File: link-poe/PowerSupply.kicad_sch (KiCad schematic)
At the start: 8 parts, among them U501 TPSM33625

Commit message: Update Library
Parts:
- C501: symbol V2_Device:C_1210_10u -> V2_Capacitor:1210_10u
- C502: symbol V2_Device:C_0603_0u1 -> V2_Capacitor:0603_0u1
- C503, C504: value 22u -> 10u; symbol V2_Device:C_1210_22u -> V2_Capacitor:1210_22u
- C505: symbol V2_Device:C_0603_1u -> V2_Capacitor:0603_1u
- R501: symbol V2_Device:R_0603_40k2 -> V2_Resistor:0603_40k2
- R502: symbol V2_Device:R_0603_10k -> V2_Resistor:0603_10k
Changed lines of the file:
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@@
 	)
 	(symbol
-		(lib_id "V2_Device:C_0603_0u1")
+		(lib_id "V2_Capacitor:0603_0u1")
 		(at 109.22 97.79 0)
 		(unit 1)
@@
 	)
 	(symbol
-		(lib_id "V2_Device:C_1210_22u")
+		(lib_id "V2_Capacitor:1210_22u")
 		(at 195.58 97.79 0)
 		(unit 1)
@@
 			)
 		)
-		(property "Value" "22u"
+		(property "Value" "10u"
 			(at 198.12 99.06 0)
 			(effects
@@
 	)
 	(symbol
-		(lib_id "V2_Device:R_0603_40k2")
+		(lib_id "V2_Resistor:0603_40k2")
 		(at 172.72 97.79 0)
 		(unit 1)
@@
 		(on_board yes)
 		(dnp no)
-		(property "Reference" "#PWR0504"
+		(property "Reference" "#PWR504"
 			(at 185.42 106.68 0)
 			(effects
@@
 			(project "power-rj45"
 				(path "/6c8448b4-b04d-47e1-934e-e40cbe27a7be/24a9dc0c-cb3c-464a-a734-f09bf949d71a"
-					(reference "#PWR0504")
+					(reference "#PWR504")
 					(unit 1)
 				)
@@
 		(on_board yes)
 		(dnp no)
-		(property "Reference" "#PWR0505"
+		(property "Reference" "#PWR505"
 			(at 195.58 106.68 0)
 			(effects
@@
 			(project "power-rj45"
 				(path "/6c8448b4-b04d-47e1-934e-e40cbe27a7be/24a9dc0c-cb3c-464a-a734-f09bf949d71a"
-					(reference "#PWR0505")
+					(reference "#PWR505")
 					(unit 1)
 				)
@@
 		(on_board yes)
 		(dnp no)
-		(property "Reference" "#PWR0501"
+		(property "Reference" "#PWR501"
 			(at 195.58 99.06 0)
 			(effects
@@
 			(project "power-rj45"
 				(path "/6c8448b4-b04d-47e1-934e-e40cbe27a7be/24a9dc0c-cb3c-464a-a734-f09bf949d71a"
-					(reference "#PWR0501")
+					(reference "#PWR501")
 					(unit 1)
 				)
@@
 		(on_board yes)
 		(dnp no)
-		(property "Reference" "#PWR0502"
+		(property "Reference" "#PWR502"
 			(at 97.79 106.68 0)
 			(effects
@@
 			(project "power-rj45"
 				(path "/6c8448b4-b04d-47e1-934e-e40cbe27a7be/24a9dc0c-cb3c-464a-a734-f09bf949d71a"
-					(reference "#PWR0502")
+					(reference "#PWR502")
 					(unit 1)
 				)
@@
 		(on_board yes)
 		(dnp no)
-		(property "Reference" "#PWR0506"
+		(property "Reference" "#PWR506"
 			(at 172.72 111.76 0)
 			(effects
@@
 			(project "power-rj45"
 				(path "/6c8448b4-b04d-47e1-934e-e40cbe27a7be/24a9dc0c-cb3c-464a-a734-f09bf949d71a"
-					(reference "#PWR0506")
+					(reference "#PWR506")
 					(unit 1)
 				)
@@
 		(on_board yes)
 		(dnp no)
-		(property "Reference" "#PWR0503"
+		(property "Reference" "#PWR503"
 			(at 109.22 106.68 0)
 			(effects
@@
 			(project "power-rj45"
 				(path "/6c8448b4-b04d-47e1-934e-e40cbe27a7be/24a9dc0c-cb3c-464a-a734-f09bf949d71a"
-					(reference "#PWR0503")
-					(unit 1)
-				)
-			)
-		)
-	)
-	(symbol
-		(lib_id "V2_Device:C_0603_1u")
+					(reference "#PWR503")
+					(unit 1)
+				)
+			)
+		)
+	)
+	(symbol
+		(lib_id "V2_Capacitor:0603_1u")
 		(at 128.27 107.95 0)
 		(unit 1)
@@
 	)
 	(symbol
-		(lib_id "V2_Device:C_1210_22u")
+		(lib_id "V2_Capacitor:1210_22u")
 		(at 185.42 97.79 0)
 		(unit 1)
@@
 			)
 		)
-		(property "Value" "22u"
+		(property "Value" "10u"
 			(at 187.96 99.06 0)
 			(effects
@@
 		(on_board yes)
 		(dnp no)
-		(property "Reference" "#PWR0507"
+		(property "Reference" "#PWR507"
 			(at 128.27 116.84 0)
 			(effects
@@
 			(project "power-rj45"
 				(path "/6c8448b4-b04d-47e1-934e-e40cbe27a7be/24a9dc0c-cb3c-464a-a734-f09bf949d71a"
-					(reference "#PWR0507")
-					(unit 1)
-				)
-			)
-		)
-	)
-	(symbol
-		(lib_id "V2_Device:R_0603_10k")
+					(reference "#PWR507")
+					(unit 1)
+				)
+			)
+		)
+	)
+	(symbol
+		(lib_id "V2_Resistor:0603_10k")
 		(at 172.72 102.87 0)
 		(unit 1)
@@
 		(on_board yes)
 		(dnp no)
-		(property "Reference" "#PWR0508"
+		(property "Reference" "#PWR508"
 			(at 148.59 121.92 0)
 			(effects
@@
 			(project "power-rj45"
 				(path "/6c8448b4-b04d-47e1-934e-e40cbe27a7be/24a9dc0c-cb3c-464a-a734-f09bf949d71a"
-					(reference "#PWR0508")
-					(unit 1)
-				)
-			)
-		)
-	)
-	(symbol
-		(lib_id "V2_Device:C_1210_10u")
+					(reference "#PWR508")
+					(unit 1)
+				)
+			)
+		)
+	)
+	(symbol
+		(lib_id "V2_Capacitor:1210_10u")
 		(at 97.79 97.79 0)
 		(unit 1)

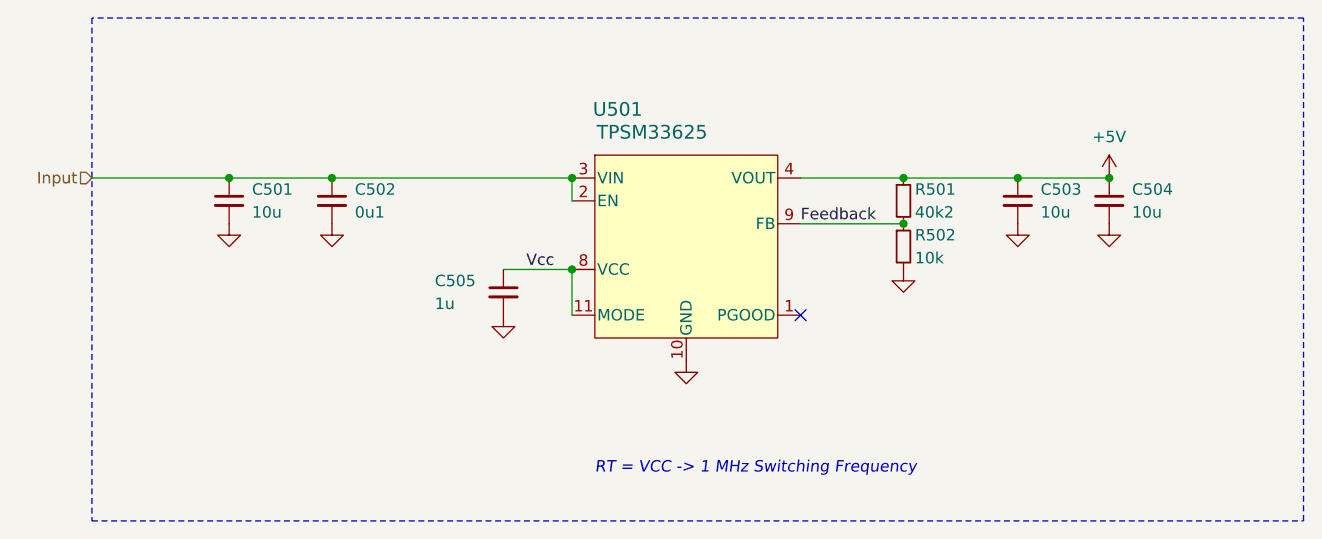
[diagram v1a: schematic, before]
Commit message: Replace step-down
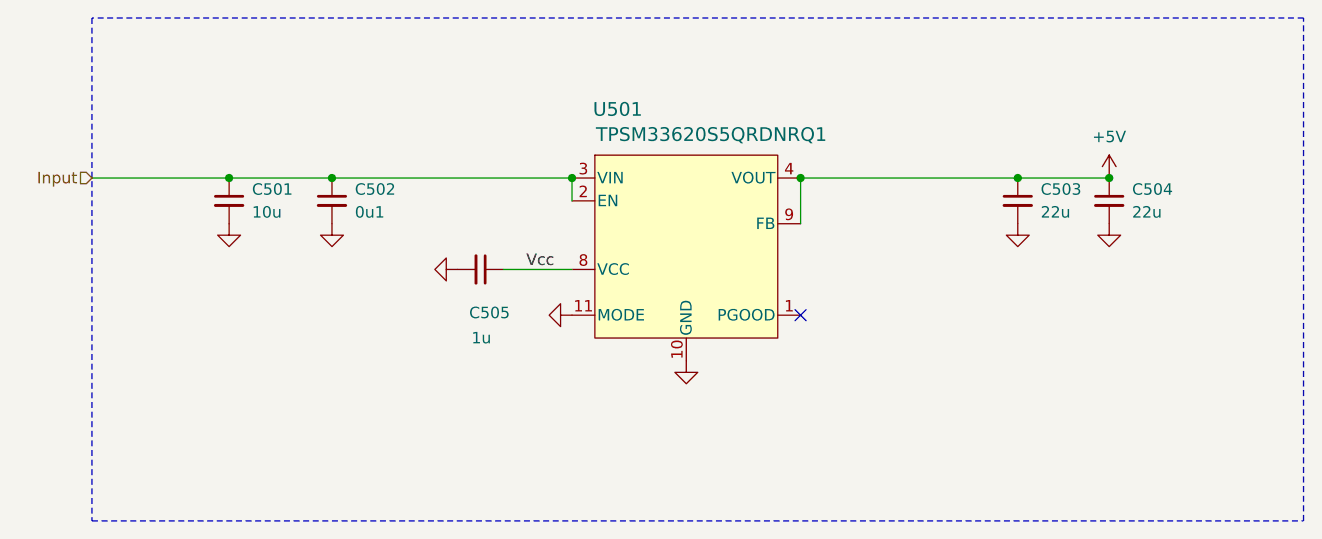
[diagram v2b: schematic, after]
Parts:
- removed R501: 40k2, V2_Resistor_SMD:R_0603, symbol V2_Resistor:0603_40k2
- removed R502: 10k, V2_Resistor_SMD:R_0603, symbol V2_Resistor:0603_10k
- C503, C504: value 10u -> 22u
- U501: value TPSM33625 -> TPSM33620S5QRDNRQ1; symbol V2_Converter_DCDC:TPSM33625RDNR -> V2_Converter_DCDC:TPSM33620S5QRDNRQ1; Mouser 595-TPSM33625RDNR -> 595-SM33620S5QRDNRQ1; Product TPSM33625RDNR -> TPSM33620S5QRDNRQ1; Rating 2.5A -> 2A
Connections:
- net Feedback is gone; now on net +5V: U501.9 (FB)
- net GND: now also U501.11 (MODE)
- net Vcc: no longer U501.11 (MODE)
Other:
- note removed: "RT = VCC -> 1 MHz Switching Frequency"
- title: Power Supply -> V2 Link PoE
- moved on the sheet: C505

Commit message: Update
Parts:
- C501: Id (none) -> Capacitor:${SYMBOL_NAME}; Mouser 810-CNA6P1X7R1H106K2 -> 810-CNC6P1X7R1H106K2; Product CNA6P1X7R1H106K250AE -> CNC6P1X7R1H106K250AE
- C502: Id (none) -> Capacitor:${SYMBOL_NAME}
- C503: renamed from C505; Id (none) -> Capacitor:${SYMBOL_NAME}
- C504: renamed from C503; Id (none) -> Capacitor:${SYMBOL_NAME}
- C505: renamed from C504; Id (none) -> Capacitor:${SYMBOL_NAME}
- U501: Id (none) -> DCDC:${SYMBOL_NAME}
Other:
- company: +5V -> Versio Duo
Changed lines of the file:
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@@
 	(title_block
 		(title "V2 Link PoE")
-		(date "2026-03-31")
+		(date "2026-04-14")
 		(rev "2026-03-31")
-		(company "+5V")
+		(company "Versio Duo")
+		(comment 1 "CAT Cable Power Supply")
 	)
 	(junction
@@
 			)
 		)
+		(property "Id" "DCDC:${SYMBOL_NAME}"
+			(at 148.59 147.32 0)
+			(hide yes)
+			(show_name no)
+			(do_not_autoplace no)
+			(effects
+				(font
+					(size 1.27 1.27)
+				)
+			)
+		)
 		(pin "1"
 		)
@@
 		(in_pos_files yes)
 		(dnp no)
-		(property "Reference" "#PWR509"
+		(property "Reference" "#PWR504"
 			(at 129.54 110.49 0)
 			(hide yes)
@@
 			(project "link-poe"
 				(path "/6c8448b4-b04d-47e1-934e-e40cbe27a7be/24a9dc0c-cb3c-464a-a734-f09bf949d71a"
-					(reference "#PWR509")
+					(reference "#PWR504")
 					(unit 1)
 				)
@@
 			)
 		)
+		(property "Id" "Capacitor:${SYMBOL_NAME}"
+			(at 109.22 113.03 0)
+			(hide yes)
+			(show_name no)
+			(do_not_autoplace no)
+			(effects
+				(font
+					(size 1.27 1.27)
+				)
+			)
+		)
 		(pin "1"
 		)
@@
 		(in_pos_files yes)
 		(dnp no)
-		(property "Reference" "C504"
+		(property "Reference" "C505"
 			(at 198.12 96.52 0)
 			(show_name no)
@@
 		(property "Rating" "25V"
 			(at 195.58 118.11 0)
+			(hide yes)
+			(show_name no)
+			(do_not_autoplace no)
+			(effects
+				(font
+					(size 1.27 1.27)
+				)
+			)
+		)
+		(property "Id" "Capacitor:${SYMBOL_NAME}"
+			(at 195.58 113.03 0)
 			(hide yes)
 			(show_name no)
@@
 			(project "link-poe"
 				(path "/6c8448b4-b04d-47e1-934e-e40cbe27a7be/24a9dc0c-cb3c-464a-a734-f09bf949d71a"
-					(reference "C504")
+					(reference "C505")
 					(unit 1)
 				)
@@
 		(in_pos_files yes)
 		(dnp no)
-		(property "Reference" "#PWR504"
+		(property "Reference" "#PWR506"
 			(at 185.42 106.68 0)
 			(hide yes)
@@
 			(project "link-poe"
 				(path "/6c8448b4-b04d-47e1-934e-e40cbe27a7be/24a9dc0c-cb3c-464a-a734-f09bf949d71a"
-					(reference "#PWR504")
+					(reference "#PWR506")
 					(unit 1)
 				)
@@
 		(in_pos_files yes)
 		(dnp no)
-		(property "Reference" "#PWR505"
+		(property "Reference" "#PWR508"
 			(at 195.58 106.68 0)
 			(hide yes)
@@
 			(project "link-poe"
 				(path "/6c8448b4-b04d-47e1-934e-e40cbe27a7be/24a9dc0c-cb3c-464a-a734-f09bf949d71a"
-					(reference "#PWR505")
+					(reference "#PWR508")
 					(unit 1)
 				)
@@
 		(in_pos_files yes)
 		(dnp no)
-		(property "Reference" "#PWR501"
+		(property "Reference" "#PWR507"
 			(at 195.58 99.06 0)
 			(hide yes)
@@
 			(project "link-poe"
 				(path "/6c8448b4-b04d-47e1-934e-e40cbe27a7be/24a9dc0c-cb3c-464a-a734-f09bf949d71a"
-					(reference "#PWR501")
+					(reference "#PWR507")
 					(unit 1)
 				)
@@
 		(in_pos_files yes)
 		(dnp no)
-		(property "Reference" "#PWR502"
+		(property "Reference" "#PWR501"
 			(at 97.79 106.68 0)
 			(hide yes)
@@
 			(project "link-poe"
 				(path "/6c8448b4-b04d-47e1-934e-e40cbe27a7be/24a9dc0c-cb3c-464a-a734-f09bf949d71a"
-					(reference "#PWR502")
+					(reference "#PWR501")
 					(unit 1)
 				)
@@
 		(in_pos_files yes)
 		(dnp no)
-		(property "Reference" "#PWR503"
+		(property "Reference" "#PWR502"
 			(at 109.22 106.68 0)
 			(hide yes)
@@
 			(project "link-poe"
 				(path "/6c8448b4-b04d-47e1-934e-e40cbe27a7be/24a9dc0c-cb3c-464a-a734-f09bf949d71a"
-					(reference "#PWR503")
+					(reference "#PWR502")
 					(unit 1)
 				)
@@
 		(in_pos_files yes)
 		(dnp no)
-		(property "Reference" "C505"
+		(property "Reference" "C503"
 			(at 124.46 110.236 90)
 			(show_name no)
@@
 		(property "Rating" "50V"
 			(at 102.87 105.41 0)
+			(hide yes)
+			(show_name no)
+			(do_not_autoplace no)
+			(effects
+				(font
+					(size 1.27 1.27)
+				)
+			)
+		)
+		(property "Id" "Capacitor:${SYMBOL_NAME}"
+			(at 110.49 105.41 0)
 			(hide yes)
 			(show_name no)
@@
 			(project "link-poe"
 				(path "/6c8448b4-b04d-47e1-934e-e40cbe27a7be/24a9dc0c-cb3c-464a-a734-f09bf949d71a"
-					(reference "C505")
+					(reference "C503")
 					(unit 1)
 				)
@@
 		(in_pos_files yes)
 		(dnp no)
-		(property "Reference" "C503"
+		(property "Reference" "C504"
 			(at 187.96 96.52 0)
 			(show_name no)
@@
 		(property "Rating" "25V"
 			(at 185.42 118.11 0)
+			(hide yes)
+			(show_name no)
+			(do_not_autoplace no)
+			(effects
+				(font
+					(size 1.27 1.27)
+				)
+			)
+		)
+		(property "Id" "Capacitor:${SYMBOL_NAME}"
+			(at 185.42 113.03 0)
 			(hide yes)
 			(show_name no)
@@
 			(project "link-poe"
 				(path "/6c8448b4-b04d-47e1-934e-e40cbe27a7be/24a9dc0c-cb3c-464a-a734-f09bf949d71a"
-					(reference "C503")
+					(reference "C504")
 					(unit 1)
 				)
@@
 		(in_pos_files yes)
 		(dnp no)
-		(property "Reference" "#PWR507"
+		(property "Reference" "#PWR503"
 			(at 116.84 105.41 0)
 			(hide yes)
@@
 			(project "link-poe"
 				(path "/6c8448b4-b04d-47e1-934e-e40cbe27a7be/24a9dc0c-cb3c-464a-a734-f09bf949d71a"
-					(reference "#PWR507")
+					(reference "#PWR503")
 					(unit 1)
 				)
@@
 		(in_pos_files yes)
 		(dnp no)
-		(property "Reference" "#PWR508"
+		(property "Reference" "#PWR505"
 			(at 148.59 121.92 0)
 			(hide yes)
@@
 			(project "link-poe"
 				(path "/6c8448b4-b04d-47e1-934e-e40cbe27a7be/24a9dc0c-cb3c-464a-a734-f09bf949d71a"
-					(reference "#PWR508")
+					(reference "#PWR505")
 					(unit 1)
 				)
@@
 			)
 		)
-		(property "Mouser" "810-CNA6P1X7R1H106K2"
+		(property "Mouser" "810-CNC6P1X7R1H106K2"
 			(at 97.79 114.3 0)
 			(hide yes)
@@
 			)
 		)
-		(property "Product" "CNA6P1X7R1H106K250AE"
+		(property "Product" "CNC6P1X7R1H106K250AE"
 			(at 97.79 115.57 0)
 			(hide yes)
@@
 			(hide yes)
 			(show_name no)
+			(do_not_autoplace no)
+			(effects
+				(font
+					(size 1.27 1.27)
+				)
+			)
+		)
+		(property "Id" "Capacitor:${SYMBOL_NAME}"
+			(at 97.79 113.03 0)
+			(hide yes)
+			(show_name no)

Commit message: Good Bye Imperial
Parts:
- C501: footprint V2_Capacitor_SMD:C_1210 -> V2_Capacitor_SMD:C_3225; symbol V2_Capacitor:1210_10u -> V2_Capacitor:3225_10u
- C502: footprint V2_Capacitor_SMD:C_0603 -> V2_Capacitor_SMD:C_1608; symbol V2_Capacitor:0603_0u1 -> V2_Capacitor:1608_0u1
- C503: footprint V2_Capacitor_SMD:C_0603 -> V2_Capacitor_SMD:C_1608; symbol V2_Capacitor:0603_1u -> V2_Capacitor:1608_1u
- C504, C505: footprint V2_Capacitor_SMD:C_1210 -> V2_Capacitor_SMD:C_3225; symbol V2_Capacitor:1210_22u -> V2_Capacitor:3225_22u
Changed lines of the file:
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@@
 	)
 	(symbol
-		(lib_id "V2_Capacitor:0603_0u1")
+		(lib_id "V2_Capacitor:1608_0u1")
 		(at 109.22 97.79 0)
 		(unit 1)
@@
 			)
 		)
-		(property "Footprint" "V2_Capacitor_SMD:C_0603"
+		(property "Footprint" "V2_Capacitor_SMD:C_1608"
 			(at 109.22 114.808 0)
 			(hide yes)
@@
 	)
 	(symbol
-		(lib_id "V2_Capacitor:1210_22u")
+		(lib_id "V2_Capacitor:3225_22u")
 		(at 195.58 97.79 0)
 		(unit 1)
@@
 			)
 		)
-		(property "Footprint" "V2_Capacitor_SMD:C_1210"
+		(property "Footprint" "V2_Capacitor_SMD:C_3225"
 			(at 195.58 114.808 0)
 			(hide yes)
@@
 	)
 	(symbol
-		(lib_id "V2_Capacitor:0603_1u")
+		(lib_id "V2_Capacitor:1608_1u")
 		(at 125.73 105.41 270)
 		(unit 1)
@@
 			)
 		)
-		(property "Footprint" "V2_Capacitor_SMD:C_0603"
+		(property "Footprint" "V2_Capacitor_SMD:C_1608"
 			(at 108.712 105.41 0)
 			(hide yes)
@@
 	)
 	(symbol
-		(lib_id "V2_Capacitor:1210_22u")
+		(lib_id "V2_Capacitor:3225_22u")
 		(at 185.42 97.79 0)
 		(unit 1)
@@
 			)
 		)
-		(property "Footprint" "V2_Capacitor_SMD:C_1210"
+		(property "Footprint" "V2_Capacitor_SMD:C_3225"
 			(at 185.42 114.808 0)
 			(hide yes)
@@
 	)
 	(symbol
-		(lib_id "V2_Capacitor:1210_10u")
+		(lib_id "V2_Capacitor:3225_10u")
 		(at 97.79 97.79 0)
 		(unit 1)
@@
 			)
 		)
-		(property "Footprint" "V2_Capacitor_SMD:C_1210"
+		(property "Footprint" "V2_Capacitor_SMD:C_3225"
 			(at 97.79 114.808 0)
 			(hide yes)
